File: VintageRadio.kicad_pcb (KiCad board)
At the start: 2 copper layers, 70 x 50 mm, 26 parts, among them J1 Potmeter, J10 Conn_01x05_Pin, J11 Conn_01x09_Pin, J12 Conn_01x08_Socket, J13 Conn_01x08_Socket, J2 PWR, J3 Out R, J4 Speakers, J5 Volume, J6 Out L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

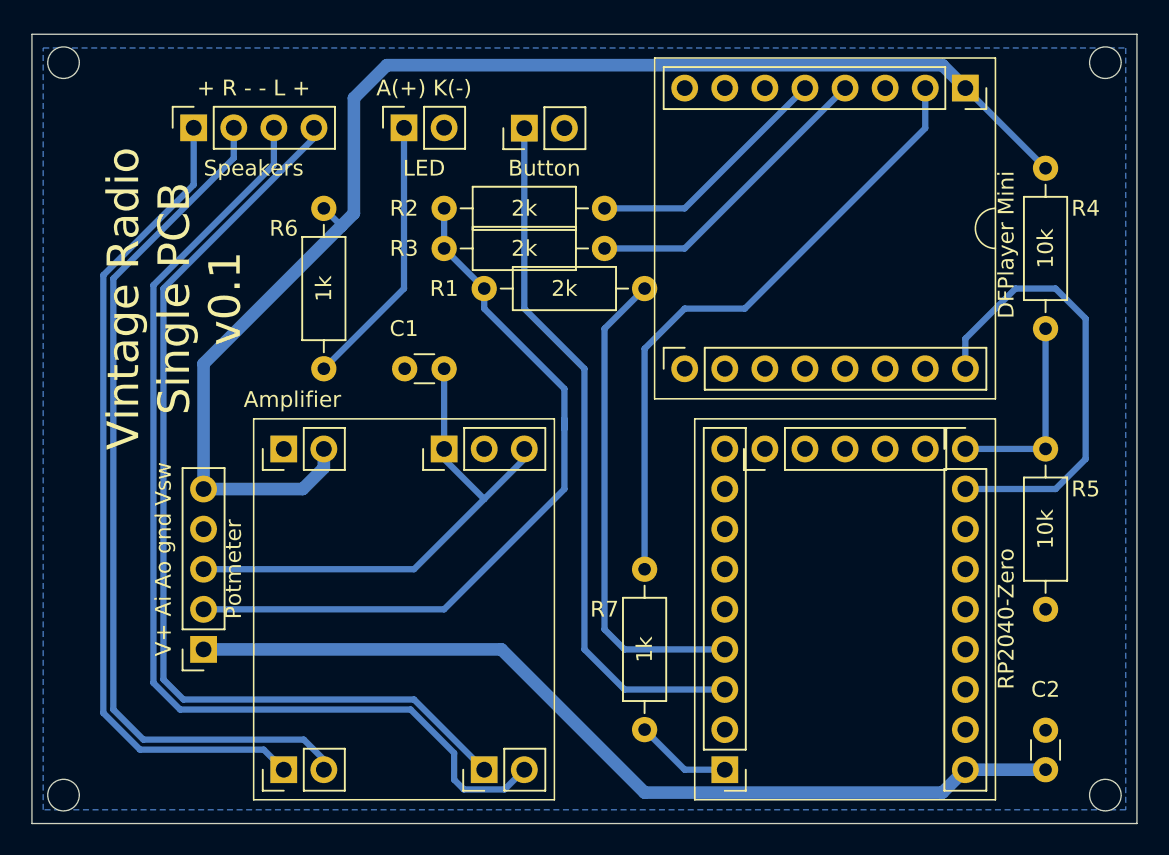
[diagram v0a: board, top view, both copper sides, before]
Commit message: better component placement
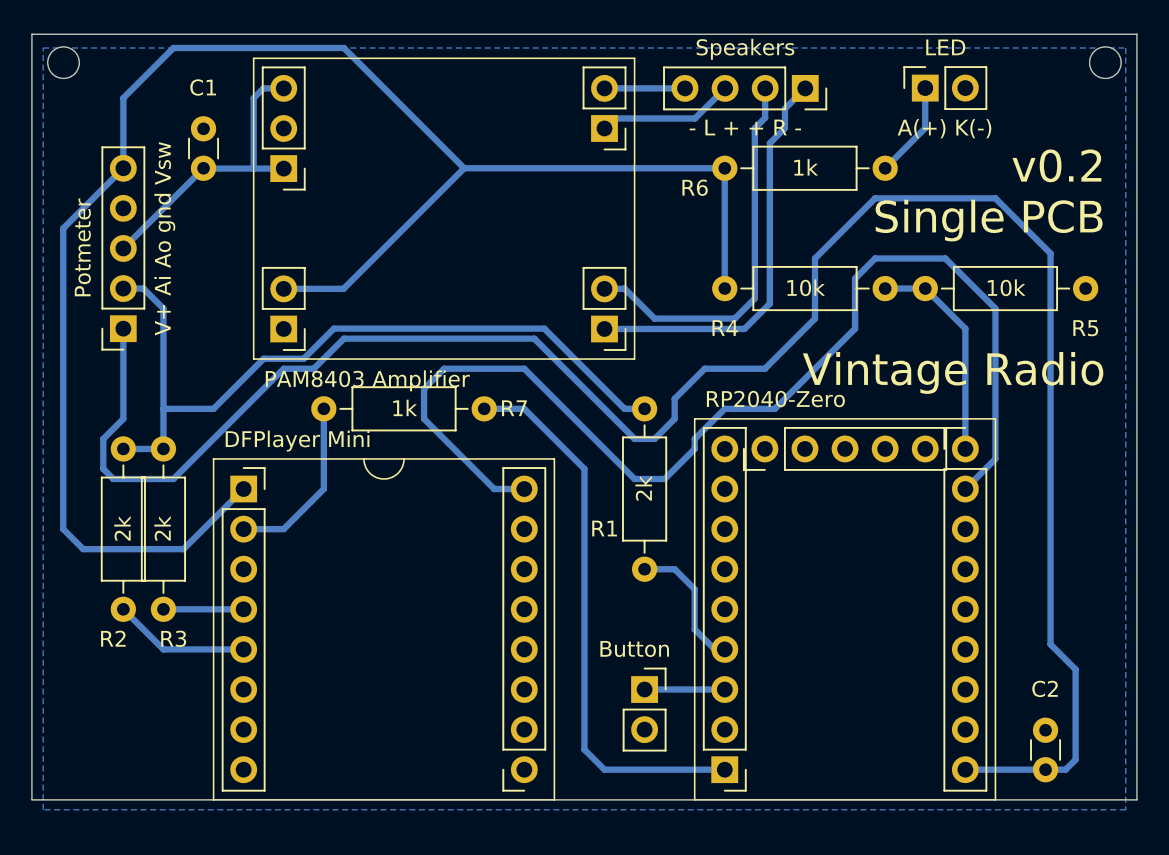
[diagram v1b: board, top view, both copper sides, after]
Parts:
- removed H3, H4: MountingHole, MountingHole:MountingHole_2mm
- J7: footprint Connector_PinHeader_2.54mm:PinHeader_1x02_P2.54mm_Vertical -> Connector_PinSocket_2.54mm:PinSocket_1x02_P2.54mm_Vertical
- moved J12 52.3 mm to (163.4, 78.8), turned to 0 degrees
- moved J6 41.3 mm to (186.3, 56.0), turned to 180 degrees
- moved J4 38.8 mm to (199.0, 53.4), turned to -90 degrees
- moved J7 36.4 mm to (188.8, 91.5), turned to 0 degrees
- moved J3 34.5 mm to (186.3, 68.7), turned to 180 degrees
- moved J9 33.1 mm to (206.6, 53.4)
- moved J13 27.4 mm to (181.2, 96.6), turned to 180 degrees
- moved R6 25.5 mm to (193.9, 58.5), turned to 0 degrees
- moved R2 25.4 mm to (155.8, 76.3), turned to -90 degrees
- moved R7 22.7 mm to (168.5, 73.7), turned to 0 degrees
- moved R3 21.8 mm to (158.3, 76.3), turned to -90 degrees
- moved R4 21.7 mm to (193.9, 66.1), turned to 0 degrees
- moved J1 20.9 mm to (155.8, 68.7)
- moved R5 20.5 mm to (216.8, 66.1), turned to 180 degrees
- moved J5 20.5 mm to (165.9, 58.5), turned to 180 degrees
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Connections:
- J6 pad 1: Net-(J4-Pin_4) -> Net-(J4-Pin_3)
- J6 pad 2: Net-(J4-Pin_3) -> Net-(J4-Pin_4)
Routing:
- net Net-(J1-Pin_1): track 57.7 -> 126.7 mm
- net Net-(J4-Pin_3): track 66.1 -> 9.60 mm
- net Net-(J4-Pin_4): track 61.6 -> 5.10 mm
- net Net-(J11-Pin_2): track 28.9 -> 71.3 mm
- net Net-(J7-Pin_1): track 44.5 -> 5.08 mm
- net Net-(J3-Pin_2): track 55.3 -> 24.4 mm
- net Net-(J8-Pin_1): track 6.13 -> 35.1 mm
- net Net-(J12-Pin_2): track 40.1 -> 11.2 mm
- net Net-(J3-Pin_1): track 52.4 -> 25.7 mm
- net Net-(J8-Pin_4): track 30.8 -> 8.67 mm
- net VCC: track 87.0 -> 107.2 mm
- net Net-(J12-Pin_4): track 19.4 -> 5.08 mm
- net Net-(J1-Pin_3): track 33.2 -> 18.9 mm
- net Net-(J9-Pin_1): track 17.4 -> 6.13 mm
- net Net-(J12-Pin_5): track 15.9 -> 8.67 mm
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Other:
- board size 70 x 50 mm -> 70 x 48.5 mm
- board text added: "PAM8403 Amplifier"
- board text added: "v0.2 Single PCB Vintage Radio"
- board text removed: "Amplifier"
- board text removed: "Vintage Radio Single PCB v0.1"
